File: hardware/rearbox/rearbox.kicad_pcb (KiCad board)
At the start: 4 copper layers, 80 x 60 mm, 366 parts, among them IC2 TPS54202HDDCR, J1 STDC14, J2 ST-LINK, J3 Conn_02x28_Top_Bottom, J4 Auxiliary, Q1 BUK6D210, Q2 BUK6D210, Q3 BUK6D210, Q4 BUK6D210, Q5 BUK6D210, Q6 BUK6D210, SW1 Reset, U1 LM4040C33FTA, U10 TLP291-4, U11 TLP291-4, U12 TLP291-4, U13 MCP6N11T-002, U14 MCP6001, U15 MCP6N11T-002, U16 MCP6001, U17 MCP6N11T-002, U18 MCP6001, U19 MCP6N11T-002, U2 STM32G473RCTx, U20 MCP6001, U21 MCP6N11T-002, U22 MCP6001, U23 MCP6N11T-002, U24 MCP6001, U25 MCP6N11T-002, U26 MCP6001, U27 MCP6N11T-002, U28 MCP6001, U29 MCP6N11T-002, U30 MCP6001, U31 NAU7802SGI, U4 TLV743P, U5 MCP2542FD, U6 MCP2542FD, U7 VND7020AJTR, U8 VND7020AJTR, U9 TCA6416ARTWR, Y1 48MHz

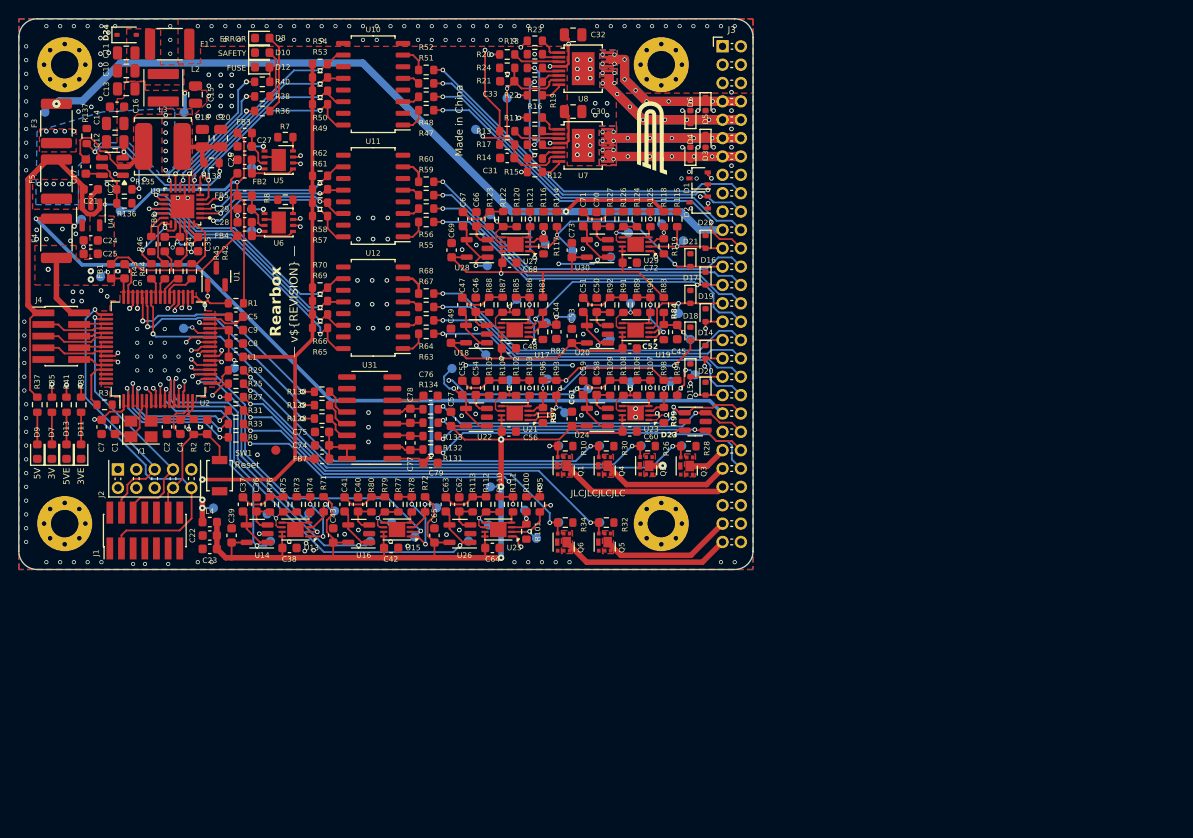
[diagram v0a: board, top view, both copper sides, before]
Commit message: Deleted measurement systems for new iteration
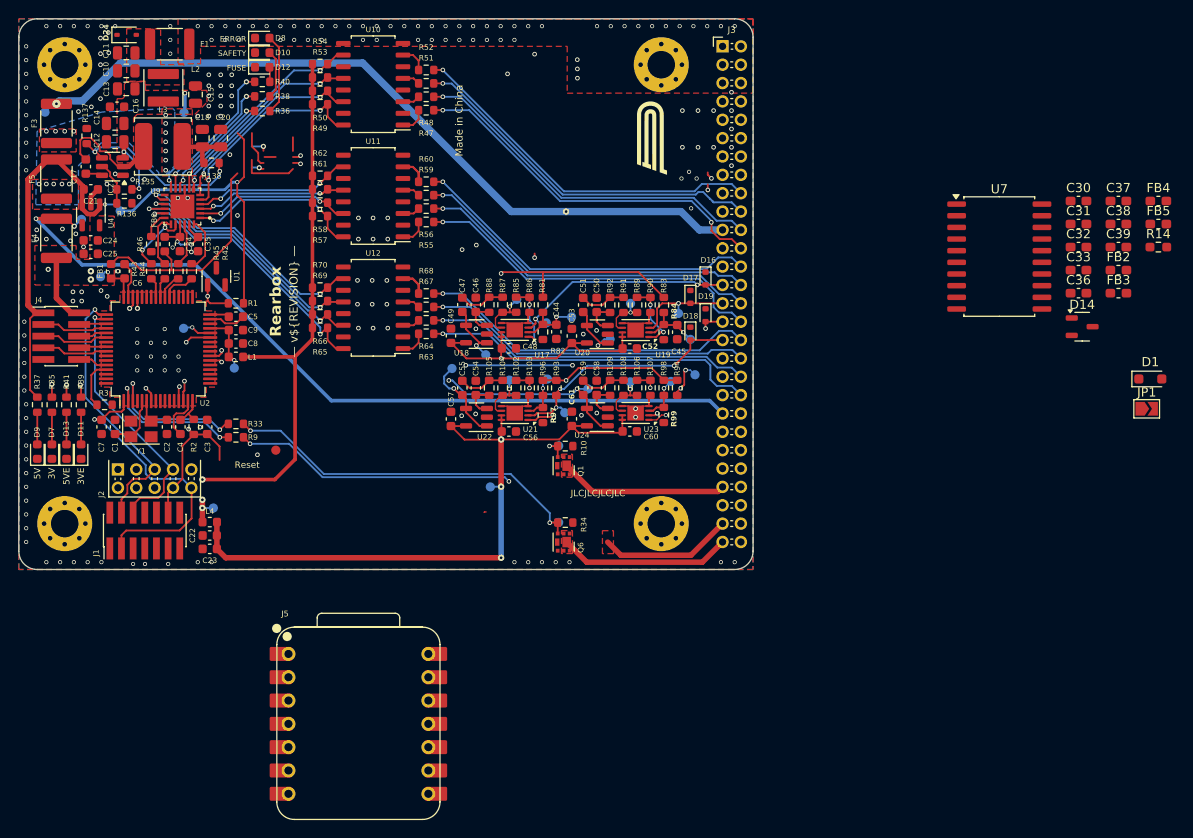
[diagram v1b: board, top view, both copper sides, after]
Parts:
- removed C26, C27, C28, C29, C40, C41, C42, C43, C62, C63, C64, C65, C66, C67, C68, C69, C70, C71, C72, C73, C75, C76, C77, C78: 100n, Capacitor_SMD:C_0603_1608Metric
- removed C74, C79: 1u, Capacitor_SMD:C_0603_1608Metric
- removed D15, D20, D21, D22: 5V, Diode_SMD:D_SOD-523
- removed D2: PESD2IVN24-U, Package_TO_SOT_SMD:SOT-323_SC-70
- removed D23: CPDT6-5V4, Package_TO_SOT_SMD:SOT-23-6
- removed D3, D4, D5, D6: PMEG3010EB, Diode_SMD:D_SOD-523
- removed FB7: 470R, Inductor_SMD:L_0603_1608Metric
- removed NT3, NT4, NT5: NetTie_2, Local_Library:NetTie-2_SMD_Pad0.2mm
- removed Q2, Q3, Q4, Q5: BUK6D210, Local_Library:Diodes_UDFN2020-6_Type-F
- removed R100, R95: 1k, Resistor_SMD:R_0603_1608Metric
- removed R101, R114, R115, R116, R118: 2k, Resistor_SMD:R_0603_1608Metric
- removed R11, R12, R128, R129, R13, R130, R15, R18, R19, R20, R21, R22, R25, R27, R29, R31, R71, R72: 100R, Resistor_SMD:R_0603_1608Metric
- removed R110, R111, R120, R121, R124, R125, R17, R24, R73, R74, R77, R78: TBD, Resistor_SMD:R_0603_1608Metric
- removed R112, R113, R122, R123, R126, R127, R75, R76, R79, R80: 3k3, Resistor_SMD:R_0603_1608Metric
- removed R117, R119: 2k7, Resistor_SMD:R_0603_1608Metric
- removed R131, R132, R133, R134: 51R, Resistor_SMD:R_0603_1608Metric
- removed R16, R23: 15k, Resistor_SMD:R_0603_1608Metric
- removed R26, R28, R30, R32: 10k, Resistor_SMD:R_0603_1608Metric
- removed R7, R8: 0R, Resistor_SMD:R_0603_1608Metric
- removed SW1: Reset, Button_Switch_SMD:SW_SPST_B3U-1000P
- removed TP12, TP13, TP14, TP15, TP17, TP18, TP19, TP20, TP21, TP22, TP24, TP25, TP26, TP27, TP28, TP29, TP30, TP31, TP48, TP49, TP50, TP51, TP52, TP53, TP54, TP55, TP56, TP57, TP58, TP59: TestPoint_Small, TestPoint:TestPoint_Pad_D1.0mm
- removed U13, U15, U25, U27, U29: MCP6N11T-002, Local_Library:TDFN-8-1EP_3x2mm_P0.5mm_EP1.80x1.65mm
- removed U14, U16, U26, U28, U30: MCP6001, Package_TO_SOT_SMD:SOT-23-5
- removed U31: NAU7802SGI, Package_SO:SOIC-16_3.9x9.9mm_P1.27mm
- removed U5, U6: MCP2542FD, Package_DFN_QFN:DFN-8-1EP_3x3mm_P0.65mm_EP1.55x2.4mm
- removed U8: VND7020AJTR, Local_Library:VND7020AJTR
- added J5: XIAO ESP32S3 Sense, Samacsys:XIAO-ESP32S3-DIP, F.Cu at (141.0, 150.8)
- added JP1: Jumper_2_Small_Bridged, Jumper:SolderJumper-2_P1.3mm_Open_TrianglePad1.0x1.5mm, F.Cu at (226.9, 116.5)
- C15, C18, C20: value 22uF -> 22u
- C16, C17: value 100nF -> 100n
- C30: footprint Capacitor_SMD:C_0805_2012Metric -> Capacitor_SMD:C_0603_1608Metric_Pad1.08x0.95mm_HandSolder
- C31: value 10n -> 100n; footprint Capacitor_SMD:C_0603_1608Metric -> Capacitor_SMD:C_0603_1608Metric_Pad1.08x0.95mm_HandSolder
- C32: value 100n -> 47u; footprint Capacitor_SMD:C_0805_2012Metric -> Capacitor_SMD:C_0603_1608Metric_Pad1.08x0.95mm_HandSolder
- C33, C36: footprint Capacitor_SMD:C_0603_1608Metric -> Capacitor_SMD:C_0603_1608Metric_Pad1.08x0.95mm_HandSolder
- C37: value 100n -> 10n; footprint Capacitor_SMD:C_0603_1608Metric -> Capacitor_SMD:C_0603_1608Metric_Pad1.08x0.95mm_HandSolder
- C38: value 100n -> 47u; footprint Capacitor_SMD:C_0603_1608Metric -> Capacitor_SMD:C_0603_1608Metric_Pad1.08x0.95mm_HandSolder
- C39: value 100n -> 220n; footprint Capacitor_SMD:C_0603_1608Metric -> Capacitor_SMD:C_0603_1608Metric_Pad1.08x0.95mm_HandSolder
- D1: value PESD2IVN24-U -> NSVRB751V40T1G; footprint Package_TO_SOT_SMD:SOT-323_SC-70 -> Diode_SMD:D_SOD-323_HandSoldering
- D14: value 5V -> 5.3V/400W; footprint Diode_SMD:D_SOD-523 -> Package_TO_SOT_SMD:SOT-23-3
- FB2, FB3, FB4, FB5: value 470R -> 2K@100MHz; footprint Inductor_SMD:L_0603_1608Metric -> Inductor_SMD:L_0603_1608Metric_Pad1.05x0.95mm_HandSolder
- R14: value 100R -> 100K; footprint Resistor_SMD:R_0603_1608Metric -> Resistor_SMD:R_0603_1608Metric_Pad0.98x0.95mm_HandSolder
- U7: value VND7020AJTR -> ADM3057ExRW; footprint Local_Library:VND7020AJTR -> Package_SO:SOIC-20W_7.5x12.8mm_P1.27mm
- moved C39 101.6 mm to (223.8, 98.9), turned to 0 degrees
- moved C37 100.9 mm to (223.8, 93.9), turned to 0 degrees
- moved FB4 99.6 mm to (228.2, 93.9)
- moved FB5 99.6 mm to (228.2, 96.4)
- moved C38 97.0 mm to (223.8, 96.4)
- moved FB3 96.8 mm to (223.8, 103.9)
- moved FB2 95.8 mm to (223.8, 101.4)
- moved C36 92.5 mm to (219.5, 103.9), turned to 0 degrees
- moved R14 68.8 mm to (228.2, 98.9)
- moved C33 65.6 mm to (219.5, 101.4), turned to 0 degrees
- moved C31 62.7 mm to (219.5, 96.4), turned to 0 degrees
- moved C32 59.7 mm to (219.5, 98.9), turned to 0 degrees
- moved C30 55.9 mm to (219.5, 93.9), turned to 0 degrees
- moved D1 53.9 mm to (227.3, 113.2), turned to 0 degrees
- moved U7 46.9 mm to (210.8, 99.9)
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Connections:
- C30 pad 1: +24V -> GND
- C30 pad 2: GND -> +5V
- C31 pad 1: /SENSE_OUT -> +3.3V
- C32 pad 1: +24V -> GND
- C32 pad 2: GND -> Net-(U7-VCC)
- C33 pad 1: /SENSE_OUT -> Net-(U7-VIO)
- C36 pad 1: Net-(U14-+) -> Net-(D14-A)
- C36 pad 2: GND -> Net-(U7-VISOIN)
- C37 pad 1: Net-(C37-Pad1) -> Net-(U7-VISOIN)
- C37 pad 2: /ANALOG_INPUT1 -> Net-(D14-A)
- C38 pad 1: +3.3VA -> Net-(D14-A)
- C38 pad 2: GND -> Net-(U7-VISOIN)
- C39 pad 1: +3.3VA -> Net-(C39-Pad1)
- C39 pad 2: GND -> Net-(U7-VISOOUT)
- D1 pad 1: CAN- -> Net-(D1-K)
- D1 pad 2: CAN+ -> +5V
- D14 pad 1: GND -> CAN+
- D14 pad 2: ANALOG_IN_RFU1 -> CAN-
- FB2 pad 1: +3.3V -> Net-(U7-VCC)
- FB2 pad 2: Net-(U5-VIO) -> +5V
- FB3 pad 1: +5V -> Net-(U7-VISOIN)
- FB3 pad 2: Net-(U5-VDD) -> Net-(U7-VISOOUT)
- FB4 pad 1: +3.3V -> Net-(D14-A)
- FB4 pad 2: Net-(U6-VIO) -> Net-(C39-Pad1)
- FB5 pad 1: +5V -> Net-(U7-VIO)
- FB5 pad 2: Net-(U6-VDD) -> +3.3V
- J3 pad 10: PUMP_OUT2 -> unconnected-(J3-Pin_10-Pad10)
- J3 pad 11: FAN_OUT_L -> unconnected-(J3-Pin_11-Pad11)
- J3 pad 12: FAN_OUT_L -> unconnected-(J3-Pin_12-Pad12)
- J3 pad 13: FAN_OUT_R -> unconnected-(J3-Pin_13-Pad13)
- J3 pad 14: FAN_OUT_R -> unconnected-(J3-Pin_14-Pad14)
- J3 pad 17: CAN2+ -> unconnected-(J3-Pin_17-Pad17)
- J3 pad 19: CAN2- -> unconnected-(J3-Pin_19-Pad19)
- J3 pad 23: POTENTIOMETER_IN_R -> unconnected-(J3-Pin_23-Pad23)
- J3 pad 25: POTENTIOMETER_IN_L -> unconnected-(J3-Pin_25-Pad25)
- J3 pad 35: ANALOG_IN_RFU1 -> unconnected-(J3-Pin_35-Pad35)
- J3 pad 37: ANALOG_IN_RFU2 -> unconnected-(J3-Pin_37-Pad37)
- J3 pad 39: MONO_TEMPERATURE_IN -> unconnected-(J3-Pin_39-Pad39)
- J3 pad 42: LOAD_CELL_IN_R- -> unconnected-(J3-Pin_42-Pad42)
- J3 pad 43: ASSI_OUT_R -> unconnected-(J3-Pin_43-Pad43)
- J3 pad 44: LOAD_CELL_IN_R+ -> unconnected-(J3-Pin_44-Pad44)
- J3 pad 45: ASSI_OUT_G -> unconnected-(J3-Pin_45-Pad45)
- J3 pad 46: LOAD_CELL_IN_L- -> unconnected-(J3-Pin_46-Pad46)
- J3 pad 47: ASSI_OUT_B -> unconnected-(J3-Pin_47-Pad47)
- J3 pad 48: LOAD_CELL_IN_L+ -> unconnected-(J3-Pin_48-Pad48)
- J3 pad 53: ASSI_OUT_BUZZER -> unconnected-(J3-Pin_53-Pad53)
- J3 pad 7: PUMP_OUT1 -> unconnected-(J3-Pin_7-Pad7)
- J3 pad 8: PUMP_OUT1 -> unconnected-(J3-Pin_8-Pad8)
- J3 pad 9: PUMP_OUT2 -> unconnected-(J3-Pin_9-Pad9)
- R14 pad 1: /SENSE_ADDRESS_IN0 -> Net-(D14-A)
- R14 pad 2: Net-(U7-SEL0) -> Net-(U7-RS)
- U2 pad 10: /ANALOG_INPUT1 -> unconnected-(U2-PC2-Pad10)
- U2 pad 11: /MONO_TEMPERATURE -> unconnected-(U2-PC3-Pad11)
- U2 pad 12: /ANALOG_INPUT2 -> unconnected-(U2-PA0-Pad12)
- U2 pad 17: /ASSI_LED_B -> unconnected-(U2-PA3-Pad17)
- U2 pad 18: /ANALOG_OFFSET1 -> unconnected-(U2-PA4-Pad18)
- U2 pad 19: /ANALOG_OFFSET2 -> unconnected-(U2-PA5-Pad19)
- U2 pad 20: /POTENTIOMETER_R -> unconnected-(U2-PA6-Pad20)
- U2 pad 21: /POTENTIOMETER_L -> unconnected-(U2-PA7-Pad21)
- U2 pad 24: /SENSE_OUT -> unconnected-(U2-PB0-Pad24)
- U2 pad 25: /SENSE_ADDRESS_IN0 -> unconnected-(U2-PB1-Pad25)
- U2 pad 26: /SENSE_ADDRESS_IN1 -> unconnected-(U2-PB2-Pad26)
- U2 pad 30: /FAN_R -> unconnected-(U2-PB10-Pad30)
- U2 pad 33: /FAN_L -> unconnected-(U2-PB11-Pad33)
- U2 pad 34: /CAN2_RX -> unconnected-(U2-PB12-Pad34)
- U2 pad 35: /CAN2_TX -> unconnected-(U2-PB13-Pad35)
- U2 pad 36: /PUMP2 -> unconnected-(U2-PB14-Pad36)
- U2 pad 37: /PUMP1 -> unconnected-(U2-PB15-Pad37)
- U2 pad 4: /ASSI_BUZZER -> /XIAO_GPIO
- U2 pad 42: /LOAD_CELL_SDIO -> unconnected-(U2-PA8-Pad42)
- U2 pad 43: /LOAD_CELL_SCLK -> unconnected-(U2-PA9-Pad43)
- U2 pad 44: /LOAD_CELL_DRDY -> /STBY_CAN
- U2 pad 58: /SENSE_ENABLE_PUMPS -> unconnected-(U2-PB5-Pad58)
- U2 pad 59: /SENSE_ENABLE_FANS -> unconnected-(U2-PB6-Pad59)
- U2 pad 8: /ASSI_LED_G -> unconnected-(U2-PC0-Pad8)
- U2 pad 9: /ASSI_LED_R -> unconnected-(U2-PC1-Pad9)
- U7 pad 1: Net-(U7-INPUT0) -> GND
- U7 pad 10: FAN_OUT_R -> GND
- U7 pad 11: FAN_OUT_R -> Net-(D14-A)
- U7 pad 12: FAN_OUT_R -> Net-(U7-RS)
- U7 pad 13: FAN_OUT_L -> CAN-
- U7 pad 14: FAN_OUT_L -> CAN+
- U7 pad 15: FAN_OUT_L -> Net-(D14-A)
- U7 pad 16: FAN_OUT_L -> Net-(U7-VISOIN)
- U7 pad 2: Net-(U7-~{FaultRST}) -> GND
- U7 pad 3: Net-(U7-SEn) -> Net-(U7-VCC)
- U7 pad 4: GND -> Net-(U7-VIO)
- U7 pad 5: Net-(U7-SEL0) -> /CAN_RX
- U7 pad 6: Net-(U7-SEL1) -> unconnected-(U7-SILENT-Pad6)
- U7 pad 7: /SENSE_OUT -> /CAN_TX
- U7 pad 8: Net-(U7-INPUT1) -> /STBY_CAN
- U7 pad 9: FAN_OUT_R -> GND
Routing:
- net /SENSE_OUT: track 76.0 -> 0.00 mm, vias 3 -> 0
- net /SENSE_ENABLE_FANS: track 71.1 -> 0.00 mm, vias 2 -> 0
- net /SENSE_ADDRESS_IN0: track 67.4 -> 0.00 mm, vias 3 -> 0
- net /SENSE_ADDRESS_IN1: track 65.3 -> 0.00 mm, vias 3 -> 0
- net /SENSE_ENABLE_PUMPS: track 61.1 -> 0.00 mm, vias 2 -> 0
- net /FAN_R: track 59.2 -> 0.00 mm, vias 2 -> 0
- net /POTENTIOMETER_R: track 58.2 -> 0.00 mm, vias 3 -> 0
- net ANALOG_IN_RFU1: track 56.7 -> 0.00 mm, vias 2 -> 0
- net /PUMP1: track 56.6 -> 0.00 mm, vias 2 -> 0
- net Net-(Q3-G): track 54.0 -> 0.00 mm, vias 2 -> 0
- net /PUMP2: track 53.7 -> 0.00 mm, vias 2 -> 0
- net /MONO_TEMPERATURE: track 53.1 -> 0.00 mm, vias 2 -> 0
- net /FAN_L: track 51.2 -> 0.00 mm, vias 2 -> 0
- net Net-(Q2-G): track 49.8 -> 0.00 mm, vias 2 -> 0
- net CAN2+: track 49.1 -> 0.00 mm, vias 2 -> 0
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- added copper zone on F.Cu, net unconnected-(J3-Pin_53-Pad53)
- removed copper zone on F.Cu, net ASSI_OUT_B
- removed copper zone on F.Cu, net ASSI_OUT_BUZZER
- removed copper zone on F.Cu, net ASSI_OUT_G
- removed copper zone on F.Cu, net ASSI_OUT_R
- removed copper zone on B.Cu, net FAN_OUT_L
- removed copper zone on F.Cu, net FAN_OUT_L
- removed copper zone on B.Cu, net FAN_OUT_R
- removed copper zone on F.Cu, net FAN_OUT_R
- removed copper zone on B.Cu, net PUMP_OUT1
- removed copper zone on F.Cu, net PUMP_OUT1
- removed copper zone on B.Cu, net PUMP_OUT2
- removed copper zone on F.Cu, net PUMP_OUT2

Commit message: Positioned new CANBUS components on PCB
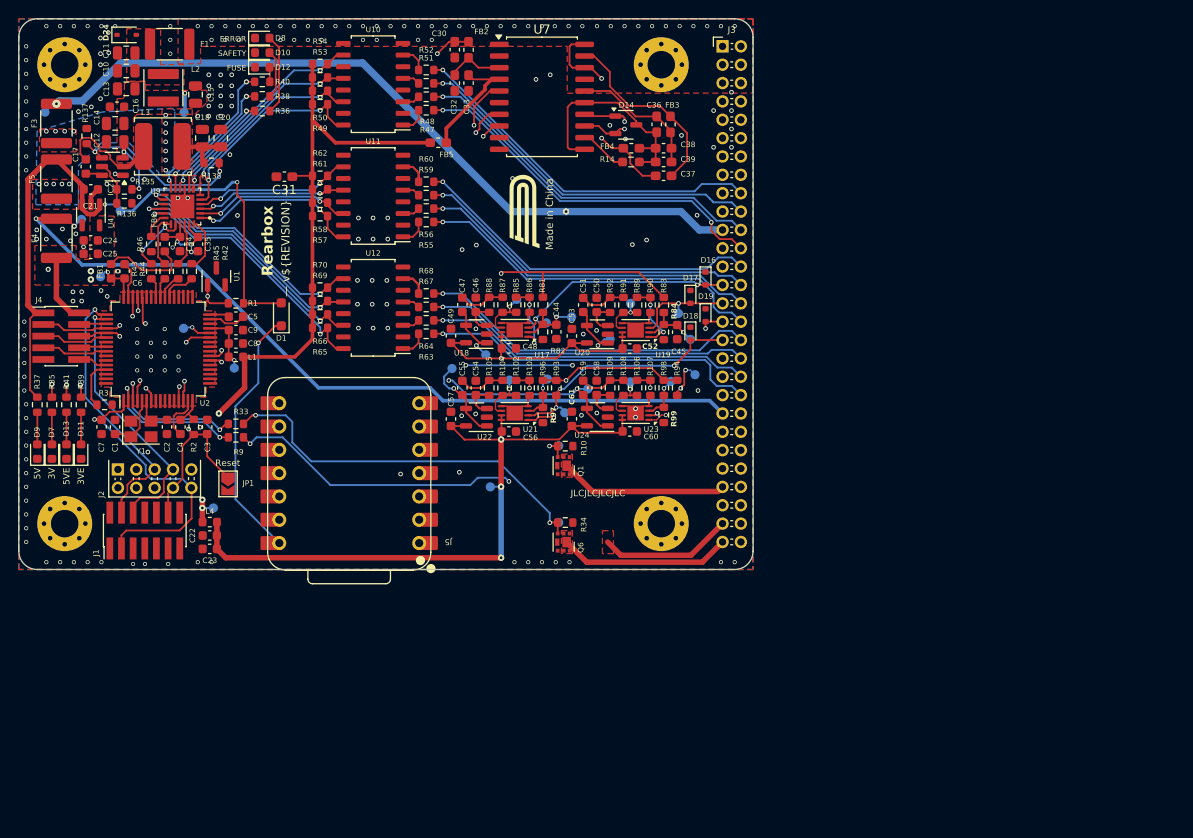
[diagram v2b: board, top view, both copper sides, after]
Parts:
- removed the REF** at (132.0, 121.0)
- moved JP1 100.4 mm to (126.8, 124.7), turned to -90 degrees
- moved D1 94.9 mm to (132.6, 106.2), turned to 90 degrees
- moved C31 86.7 mm to (132.9, 91.2), turned to 180 degrees
- moved FB5 79.0 mm to (149.7, 87.5), turned to 180 degrees
- moved FB2 74.8 mm to (153.0, 77.4), turned to 90 degrees
- moved C32 70.3 mm to (151.5, 81.0), turned to 90 degrees
- moved C30 69.9 mm to (151.5, 77.4), turned to 90 degrees
- moved C33 69.5 mm to (153.0, 81.0), turned to -90 degrees
- moved R14 58.2 mm to (170.7, 89.6), turned to 180 degrees
- moved FB4 57.7 mm to (170.7, 88.1), turned to 180 degrees
- moved D14 54.4 mm to (170.1, 85.5)
- moved U7 52.8 mm to (161.0, 82.5)
- moved FB3 52.2 mm to (175.0, 85.5), turned to 90 degrees
- moved C38 50.2 mm to (174.2, 88.1)
- moved C39 50.2 mm to (174.2, 91.1)
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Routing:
- net /STBY_CAN: track 0.00 -> 50.8 mm, vias 0 -> 2
- net UART_TX: track 7.16 -> 45.9 mm, vias 0 -> 1
- net /XIAO_GPIO: track 0.00 -> 34.9 mm, vias 0 -> 1
- net CAN+: track 51.7 -> 18.0 mm, vias 2 -> 1
- net CAN-: track 51.5 -> 20.5 mm, vias 2 -> 1
- net +5V: track 74.2 -> 103.9 mm, vias 2 -> 3
- net /CAN_RX: track 23.4 -> 52.7 mm
- net Net-(D1-K): track 0.00 -> 28.3 mm, vias 0 -> 1
- net Net-(D14-A): track 0.00 -> 25.0 mm
- net /CAN_TX: track 26.8 -> 51.5 mm
- net UART_RX: track 3.07 -> 26.2 mm, vias 0 -> 1
- net Net-(C39-Pad1): track 0.00 -> 22.5 mm, vias 0 -> 2
- net Net-(U7-VISOOUT): track 0.00 -> 20.9 mm
- net Net-(U7-VISOIN): track 0.00 -> 14.9 mm
- net Net-(U7-VIO): track 0.00 -> 13.3 mm
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
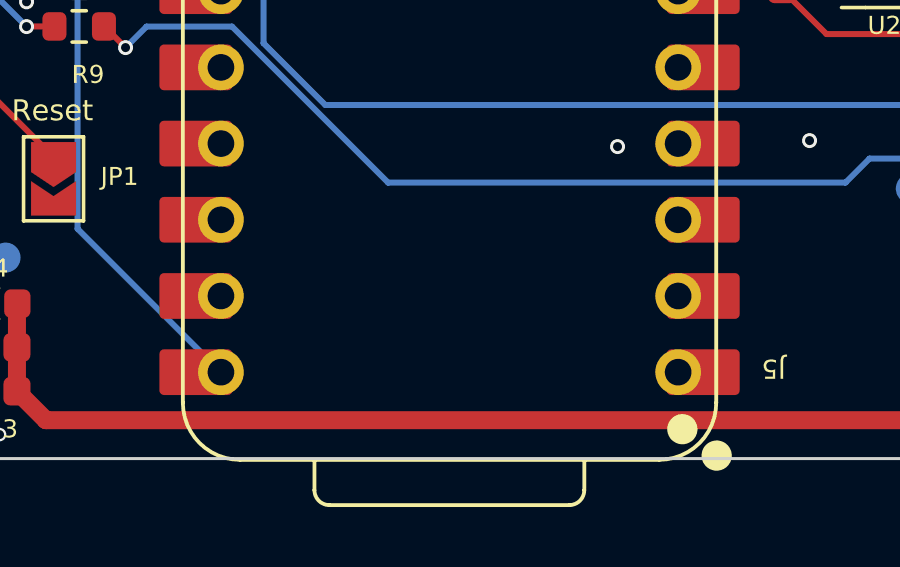
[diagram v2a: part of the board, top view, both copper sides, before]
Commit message: Fixed problematic silkscreen placements
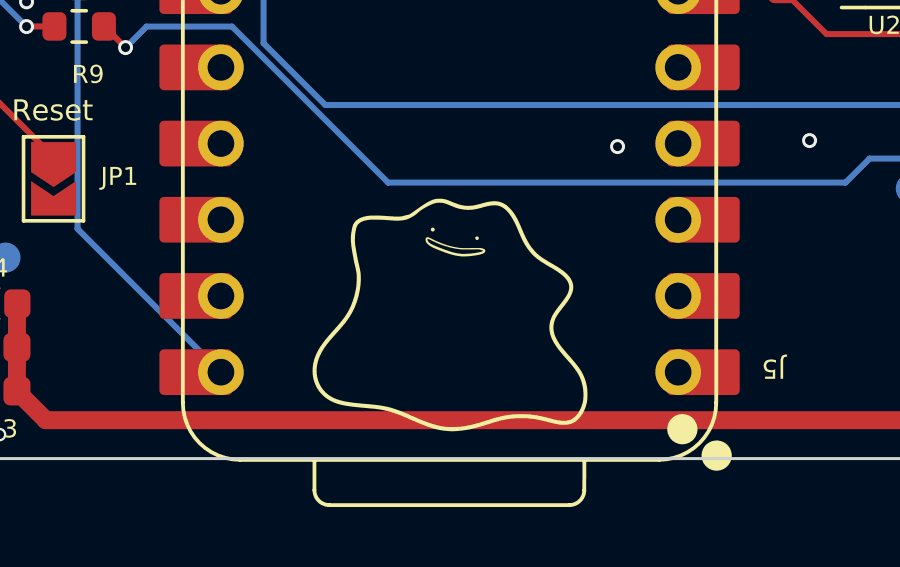
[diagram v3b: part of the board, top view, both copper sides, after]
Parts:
- added G***: LOGO, LOGO, F.Cu at (140.0, 129.0)
